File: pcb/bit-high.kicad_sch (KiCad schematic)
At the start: 5 parts, among them Q1 2N7002b, Q2 2N7002b

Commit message: Bit low/high.
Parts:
- renumbered C5 to C19, Q1 to Q707, Q2 to Q708, R1 to R299, R2 to R300
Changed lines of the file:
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@@
     (effects (font (size 1.27 1.27)) (justify left))
   )
-  (symbol (lib_id "power:VCC") (at 184.15 44.45 0) (unit 1)
+  (symbol (lib_id "power:VCC") (at 184.15 44.45 0)
     (in_bom yes) (on_board yes)
-    (property "Reference" "#PWR034" (id 0) (at 184.15 48.26 0)
+    (property "Reference" "#PWR0618" (id 0) (at 184.15 48.26 0)
       (effects (font (size 1.27 1.27)) hide)
     )
@@
     (pin "1")
   )
-  (symbol (lib_id "power:VCC") (at 200.66 40.64 0) (unit 1)
+  (symbol (lib_id "power:VCC") (at 200.66 40.64 0)
     (in_bom yes) (on_board yes)
-    (property "Reference" "#PWR033" (id 0) (at 200.66 44.45 0)
+    (property "Reference" "#PWR0617" (id 0) (at 200.66 44.45 0)
       (effects (font (size 1.27 1.27)) hide)
     )
@@
     (pin "1")
   )
-  (symbol (lib_id "power:VCC") (at 220.98 71.12 0) (unit 1)
+  (symbol (lib_id "power:VCC") (at 220.98 71.12 0)
     (in_bom yes) (on_board yes)
-    (property "Reference" "#PWR036" (id 0) (at 220.98 74.93 0)
+    (property "Reference" "#PWR0620" (id 0) (at 220.98 74.93 0)
       (effects (font (size 1.27 1.27)) hide)
     )
@@
     (pin "1")
   )
-  (symbol (lib_id "power:GND") (at 184.15 52.07 0) (unit 1)
+  (symbol (lib_id "power:GND") (at 184.15 52.07 0)
     (in_bom yes) (on_board yes)
-    (property "Reference" "#PWR035" (id 0) (at 184.15 58.42 0)
+    (property "Reference" "#PWR0619" (id 0) (at 184.15 58.42 0)
       (effects (font (size 1.27 1.27)) hide)
     )
@@
     (pin "1")
   )
-  (symbol (lib_id "power:GND") (at 220.98 109.22 0) (unit 1)
+  (symbol (lib_id "power:GND") (at 220.98 109.22 0)
     (in_bom yes) (on_board yes)
-    (property "Reference" "#PWR037" (id 0) (at 220.98 115.57 0)
+    (property "Reference" "#PWR0621" (id 0) (at 220.98 115.57 0)
       (effects (font (size 1.27 1.27)) hide)
     )
@@
     (pin "1")
   )
-  (symbol (lib_id "Device:R") (at 200.66 44.45 0) (unit 1)
+  (symbol (lib_id "Device:R") (at 200.66 44.45 0)
     (in_bom yes) (on_board yes)
-    (property "Reference" "R1" (id 0) (at 202.438 43.2816 0)
+    (property "Reference" "R299" (id 0) (at 202.438 43.2816 0)
       (effects (font (size 1.27 1.27)) (justify left))
     )
@@
     (pin "2")
   )
-  (symbol (lib_id "Device:R") (at 220.98 74.93 0) (unit 1)
+  (symbol (lib_id "Device:R") (at 220.98 74.93 0)
     (in_bom yes) (on_board yes)
-    (property "Reference" "R2" (id 0) (at 222.758 73.7616 0)
+    (property "Reference" "R300" (id 0) (at 222.758 73.7616 0)
       (effects (font (size 1.27 1.27)) (justify left))
     )
@@
     (pin "2")
   )
-  (symbol (lib_id "Device:C") (at 184.15 48.26 0) (unit 1)
+  (symbol (lib_id "Device:C") (at 184.15 48.26 0)
     (in_bom yes) (on_board yes)
-    (property "Reference" "C5" (id 0) (at 187.071 47.0916 0)
+    (property "Reference" "C19" (id 0) (at 187.071 47.0916 0)
       (effects (font (size 1.27 1.27)) (justify left))
     )
@@
     (pin "2")
   )
-  (symbol (lib_id "Transistor_FET:2N7002") (at 218.44 93.98 0) (unit 1)
+  (symbol (lib_id "Transistor_FET:2N7002") (at 218.44 93.98 0)
     (in_bom yes) (on_board yes)
-    (property "Reference" "Q1" (id 0) (at 223.6724 92.8116 0)
+    (property "Reference" "Q707" (id 0) (at 223.6724 92.8116 0)
       (effects (font (size 1.27 1.27)) (justify left))
     )
@@
     (pin "3")
   )
-  (symbol (lib_id "Transistor_FET:2N7002") (at 218.44 104.14 0) (unit 1)
+  (symbol (lib_id "Transistor_FET:2N7002") (at 218.44 104.14 0)
     (in_bom yes) (on_board yes)
-    (property "Reference" "Q2" (id 0) (at 223.6724 102.9716 0)
+    (property "Reference" "Q708" (id 0) (at 223.6724 102.9716 0)
       (effects (font (size 1.27 1.27)) (justify left))
     )

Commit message: XH/XL.
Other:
- sheet X Register: file xreg.kicad_sch -> xhreg.kicad_sch
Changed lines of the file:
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@@
       (effects (font (size 1.27 1.27)) (justify left bottom))
     )
-    (property "Sheet file" "xreg.kicad_sch" (id 1) (at 110.49 75.4385 0)
+    (property "Sheet file" "xhreg.kicad_sch" (id 1) (at 110.49 75.439 0)
       (effects (font (size 1.27 1.27)) (justify left top))
     )

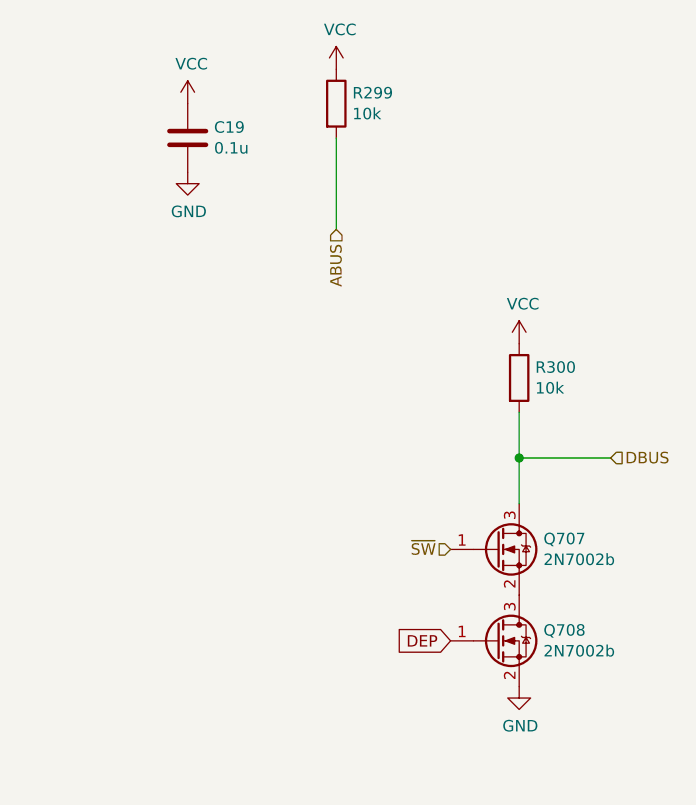
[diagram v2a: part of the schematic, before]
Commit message: Fix UUIDs.
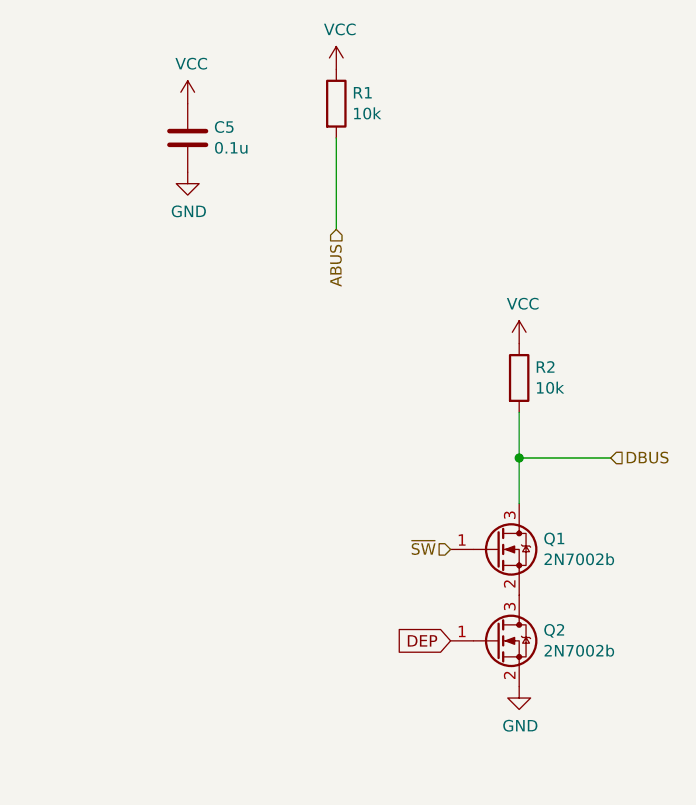
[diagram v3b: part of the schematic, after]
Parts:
- removed C19: 0.1u, Capacitor_SMD:C_0805_2012Metric, symbol Device:C
- removed Q707, Q708: 2N7002b, Package_TO_SOT_SMD:SOT-23, symbol Transistor_FET:2N7002
- removed R299, R300: 10k, Resistor_SMD:R_0805_2012Metric, symbol Device:R
- added C5: 0.1u, Capacitor_SMD:C_0805_2012Metric, symbol Device:C
- added Q1, Q2: 2N7002b, Package_TO_SOT_SMD:SOT-23, symbol Transistor_FET:2N7002
- added R1, R2: 10k, Resistor_SMD:R_0805_2012Metric, symbol Device:R
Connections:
- net ABUS: now also R1.2
- net DBUS: now also Q1.3 (D), R2.2
- net DEP: now also Q2.1 (G)
- net GND: now also C5.2, Q2.2 (S)
- net VCC: now also C5.1, R1.1, R2.1
- net ~SW: now also Q1.1 (G)
- new net: Q1.2 (S), Q2.3 (D)
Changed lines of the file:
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@@
   (symbol (lib_id "power:VCC") (at 184.15 44.45 0)
     (in_bom yes) (on_board yes)
-    (property "Reference" "#PWR0618" (id 0) (at 184.15 48.26 0)
+    (property "Reference" "#PWR020" (id 0) (at 184.15 48.26 0)
       (effects (font (size 1.27 1.27)) hide)
     )
@@
   (symbol (lib_id "power:VCC") (at 200.66 40.64 0)
     (in_bom yes) (on_board yes)
-    (property "Reference" "#PWR0617" (id 0) (at 200.66 44.45 0)
+    (property "Reference" "#PWR019" (id 0) (at 200.66 44.45 0)
       (effects (font (size 1.27 1.27)) hide)
     )
@@
   (symbol (lib_id "power:VCC") (at 220.98 71.12 0)
     (in_bom yes) (on_board yes)
-    (property "Reference" "#PWR0620" (id 0) (at 220.98 74.93 0)
+    (property "Reference" "#PWR022" (id 0) (at 220.98 74.93 0)
       (effects (font (size 1.27 1.27)) hide)
     )
@@
   (symbol (lib_id "power:GND") (at 184.15 52.07 0)
     (in_bom yes) (on_board yes)
-    (property "Reference" "#PWR0619" (id 0) (at 184.15 58.42 0)
+    (property "Reference" "#PWR021" (id 0) (at 184.15 58.42 0)
       (effects (font (size 1.27 1.27)) hide)
     )
@@
   (symbol (lib_id "power:GND") (at 220.98 109.22 0)
     (in_bom yes) (on_board yes)
-    (property "Reference" "#PWR0621" (id 0) (at 220.98 115.57 0)
+    (property "Reference" "#PWR023" (id 0) (at 220.98 115.57 0)
       (effects (font (size 1.27 1.27)) hide)
     )
@@
   (symbol (lib_id "Device:R") (at 200.66 44.45 0)
     (in_bom yes) (on_board yes)
-    (property "Reference" "R299" (id 0) (at 202.438 43.2816 0)
+    (property "Reference" "R1" (id 0) (at 202.438 43.2816 0)
       (effects (font (size 1.27 1.27)) (justify left))
     )
@@
   (symbol (lib_id "Device:R") (at 220.98 74.93 0)
     (in_bom yes) (on_board yes)
-    (property "Reference" "R300" (id 0) (at 222.758 73.7616 0)
+    (property "Reference" "R2" (id 0) (at 222.758 73.7616 0)
       (effects (font (size 1.27 1.27)) (justify left))
     )
@@
   (symbol (lib_id "Device:C") (at 184.15 48.26 0)
     (in_bom yes) (on_board yes)
-    (property "Reference" "C19" (id 0) (at 187.071 47.0916 0)
+    (property "Reference" "C5" (id 0) (at 187.071 47.0916 0)
       (effects (font (size 1.27 1.27)) (justify left))
     )
@@
   (symbol (lib_id "Transistor_FET:2N7002") (at 218.44 93.98 0)
     (in_bom yes) (on_board yes)
-    (property "Reference" "Q707" (id 0) (at 223.6724 92.8116 0)
+    (property "Reference" "Q1" (id 0) (at 223.6724 92.8116 0)
       (effects (font (size 1.27 1.27)) (justify left))
     )
@@
   (symbol (lib_id "Transistor_FET:2N7002") (at 218.44 104.14 0)
     (in_bom yes) (on_board yes)
-    (property "Reference" "Q708" (id 0) (at 223.6724 102.9716 0)
+    (property "Reference" "Q2" (id 0) (at 223.6724 102.9716 0)
       (effects (font (size 1.27 1.27)) (justify left))
     )

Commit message: New reset.
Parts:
- renumbered C5 to C18, Q1 to Q698, Q2 to Q699, R1 to R298, R2 to R299
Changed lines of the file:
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@@
   (symbol (lib_id "power:VCC") (at 184.15 44.45 0)
     (in_bom yes) (on_board yes)
-    (property "Reference" "#PWR020" (id 0) (at 184.15 48.26 0)
+    (property "Reference" "#PWR0596" (id 0) (at 184.15 48.26 0)
       (effects (font (size 1.27 1.27)) hide)
     )
@@
   (symbol (lib_id "power:VCC") (at 200.66 40.64 0)
     (in_bom yes) (on_board yes)
-    (property "Reference" "#PWR019" (id 0) (at 200.66 44.45 0)
+    (property "Reference" "#PWR0595" (id 0) (at 200.66 44.45 0)
       (effects (font (size 1.27 1.27)) hide)
     )
@@
   (symbol (lib_id "power:VCC") (at 220.98 71.12 0)
     (in_bom yes) (on_board yes)
-    (property "Reference" "#PWR022" (id 0) (at 220.98 74.93 0)
+    (property "Reference" "#PWR0598" (id 0) (at 220.98 74.93 0)
       (effects (font (size 1.27 1.27)) hide)
     )
@@
   (symbol (lib_id "power:GND") (at 184.15 52.07 0)
     (in_bom yes) (on_board yes)
-    (property "Reference" "#PWR021" (id 0) (at 184.15 58.42 0)
+    (property "Reference" "#PWR0597" (id 0) (at 184.15 58.42 0)
       (effects (font (size 1.27 1.27)) hide)
     )
@@
   (symbol (lib_id "power:GND") (at 220.98 109.22 0)
     (in_bom yes) (on_board yes)
-    (property "Reference" "#PWR023" (id 0) (at 220.98 115.57 0)
+    (property "Reference" "#PWR0599" (id 0) (at 220.98 115.57 0)
       (effects (font (size 1.27 1.27)) hide)
     )
@@
   (symbol (lib_id "Device:R") (at 200.66 44.45 0)
     (in_bom yes) (on_board yes)
-    (property "Reference" "R1" (id 0) (at 202.438 43.2816 0)
+    (property "Reference" "R298" (id 0) (at 202.438 43.2816 0)
       (effects (font (size 1.27 1.27)) (justify left))
     )
@@
   (symbol (lib_id "Device:R") (at 220.98 74.93 0)
     (in_bom yes) (on_board yes)
-    (property "Reference" "R2" (id 0) (at 222.758 73.7616 0)
+    (property "Reference" "R299" (id 0) (at 222.758 73.7616 0)
       (effects (font (size 1.27 1.27)) (justify left))
     )
@@
   (symbol (lib_id "Device:C") (at 184.15 48.26 0)
     (in_bom yes) (on_board yes)
-    (property "Reference" "C5" (id 0) (at 187.071 47.0916 0)
+    (property "Reference" "C18" (id 0) (at 187.071 47.0916 0)
       (effects (font (size 1.27 1.27)) (justify left))
     )
@@
   (symbol (lib_id "Transistor_FET:2N7002") (at 218.44 93.98 0)
     (in_bom yes) (on_board yes)
-    (property "Reference" "Q1" (id 0) (at 223.6724 92.8116 0)
+    (property "Reference" "Q698" (id 0) (at 223.6724 92.8116 0)
       (effects (font (size 1.27 1.27)) (justify left))
     )
@@
   (symbol (lib_id "Transistor_FET:2N7002") (at 218.44 104.14 0)
     (in_bom yes) (on_board yes)
-    (property "Reference" "Q2" (id 0) (at 223.6724 102.9716 0)
+    (property "Reference" "Q699" (id 0) (at 223.6724 102.9716 0)
       (effects (font (size 1.27 1.27)) (justify left))
     )

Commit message: Some fixes.
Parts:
- renumbered C18 to C22, Q698 to Q695, Q699 to Q696, R298 to R302, R299 to R303
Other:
- sheet S Register ports: added CLR; removed none
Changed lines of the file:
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@@
+    (stroke (width 0) (type solid) (color 0 0 0 0))
+  )
+  (wire (pts (xy 104.14 113.03) (xy 110.49 113.03))
     (stroke (width 0) (type solid) (color 0 0 0 0))
   )
@@
   (symbol (lib_id "power:VCC") (at 184.15 44.45 0)
     (in_bom yes) (on_board yes)
-    (property "Reference" "#PWR0596" (id 0) (at 184.15 48.26 0)
+    (property "Reference" "#PWR0607" (id 0) (at 184.15 48.26 0)
       (effects (font (size 1.27 1.27)) hide)
     )
@@
   (symbol (lib_id "power:VCC") (at 200.66 40.64 0)
     (in_bom yes) (on_board yes)
-    (property "Reference" "#PWR0595" (id 0) (at 200.66 44.45 0)
+    (property "Reference" "#PWR0606" (id 0) (at 200.66 44.45 0)
       (effects (font (size 1.27 1.27)) hide)
     )
@@
   (symbol (lib_id "power:VCC") (at 220.98 71.12 0)
     (in_bom yes) (on_board yes)
-    (property "Reference" "#PWR0598" (id 0) (at 220.98 74.93 0)
+    (property "Reference" "#PWR0609" (id 0) (at 220.98 74.93 0)
       (effects (font (size 1.27 1.27)) hide)
     )
@@
     (pin "1")
   )
+  (symbol (lib_id "power:GND") (at 104.14 113.03 0)
+    (in_bom yes) (on_board yes)
+    (property "Reference" "#PWR0611" (id 0) (at 104.14 119.38 0)
+      (effects (font (size 1.27 1.27)) hide)
+    )
+    (property "Value" "GND" (id 1) (at 104.267 117.4242 0))
+    (property "Footprint" "" (id 2) (at 104.14 113.03 0)
+      (effects (font (size 1.27 1.27)) hide)
+    )
+    (property "Datasheet" "" (id 3) (at 104.14 113.03 0)
+      (effects (font (size 1.27 1.27)) hide)
+    )
+    (pin "1")
+  )
   (symbol (lib_id "power:GND") (at 184.15 52.07 0)
     (in_bom yes) (on_board yes)
-    (property "Reference" "#PWR0597" (id 0) (at 184.15 58.42 0)
+    (property "Reference" "#PWR0608" (id 0) (at 184.15 58.42 0)
       (effects (font (size 1.27 1.27)) hide)
     )
@@
   (symbol (lib_id "power:GND") (at 220.98 109.22 0)
     (in_bom yes) (on_board yes)
-    (property "Reference" "#PWR0599" (id 0) (at 220.98 115.57 0)
+    (property "Reference" "#PWR0610" (id 0) (at 220.98 115.57 0)
       (effects (font (size 1.27 1.27)) hide)
     )
@@
   (symbol (lib_id "Device:R") (at 200.66 44.45 0)
     (in_bom yes) (on_board yes)
-    (property "Reference" "R298" (id 0) (at 202.438 43.2816 0)
+    (property "Reference" "R302" (id 0) (at 202.438 43.2816 0)
       (effects (font (size 1.27 1.27)) (justify left))
     )
@@
   (symbol (lib_id "Device:R") (at 220.98 74.93 0)
     (in_bom yes) (on_board yes)
-    (property "Reference" "R299" (id 0) (at 222.758 73.7616 0)
+    (property "Reference" "R303" (id 0) (at 222.758 73.7616 0)
       (effects (font (size 1.27 1.27)) (justify left))
     )
@@
   (symbol (lib_id "Device:C") (at 184.15 48.26 0)
     (in_bom yes) (on_board yes)
-    (property "Reference" "C18" (id 0) (at 187.071 47.0916 0)
+    (property "Reference" "C22" (id 0) (at 187.071 47.0916 0)
       (effects (font (size 1.27 1.27)) (justify left))
     )
@@
   (symbol (lib_id "Transistor_FET:2N7002") (at 218.44 93.98 0)
     (in_bom yes) (on_board yes)
-    (property "Reference" "Q698" (id 0) (at 223.6724 92.8116 0)
+    (property "Reference" "Q695" (id 0) (at 223.6724 92.8116 0)
       (effects (font (size 1.27 1.27)) (justify left))
     )
@@
   (symbol (lib_id "Transistor_FET:2N7002") (at 218.44 104.14 0)
     (in_bom yes) (on_board yes)
-    (property "Reference" "Q699" (id 0) (at 223.6724 102.9716 0)
+    (property "Reference" "Q696" (id 0) (at 223.6724 102.9716 0)
       (effects (font (size 1.27 1.27)) (justify left))
     )
@@
       (effects (font (size 1.27 1.27)) (justify left))
     )
+    (pin "CLR" input (at 110.49 113.03 180)
+      (effects (font (size 1.27 1.27)) (justify left))
+    )

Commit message: Faster.
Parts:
- renumbered C22 to C21, Q695 to Q693, Q696 to Q694, R302 to R300, R303 to R301
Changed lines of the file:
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@@
   (symbol (lib_id "power:VCC") (at 184.15 44.45 0)
     (in_bom yes) (on_board yes)
-    (property "Reference" "#PWR0607" (id 0) (at 184.15 48.26 0)
+    (property "Reference" "#PWR0604" (id 0) (at 184.15 48.26 0)
       (effects (font (size 1.27 1.27)) hide)
     )
@@
   (symbol (lib_id "power:VCC") (at 200.66 40.64 0)
     (in_bom yes) (on_board yes)
-    (property "Reference" "#PWR0606" (id 0) (at 200.66 44.45 0)
+    (property "Reference" "#PWR0603" (id 0) (at 200.66 44.45 0)
       (effects (font (size 1.27 1.27)) hide)
     )
@@
   (symbol (lib_id "power:VCC") (at 220.98 71.12 0)
     (in_bom yes) (on_board yes)
-    (property "Reference" "#PWR0609" (id 0) (at 220.98 74.93 0)
+    (property "Reference" "#PWR0606" (id 0) (at 220.98 74.93 0)
       (effects (font (size 1.27 1.27)) hide)
     )
@@
   (symbol (lib_id "power:GND") (at 104.14 113.03 0)
     (in_bom yes) (on_board yes)
-    (property "Reference" "#PWR0611" (id 0) (at 104.14 119.38 0)
+    (property "Reference" "#PWR0608" (id 0) (at 104.14 119.38 0)
       (effects (font (size 1.27 1.27)) hide)
     )
@@
   (symbol (lib_id "power:GND") (at 184.15 52.07 0)
     (in_bom yes) (on_board yes)
-    (property "Reference" "#PWR0608" (id 0) (at 184.15 58.42 0)
+    (property "Reference" "#PWR0605" (id 0) (at 184.15 58.42 0)
       (effects (font (size 1.27 1.27)) hide)
     )
@@
   (symbol (lib_id "power:GND") (at 220.98 109.22 0)
     (in_bom yes) (on_board yes)
-    (property "Reference" "#PWR0610" (id 0) (at 220.98 115.57 0)
+    (property "Reference" "#PWR0607" (id 0) (at 220.98 115.57 0)
       (effects (font (size 1.27 1.27)) hide)
     )
@@
   (symbol (lib_id "Device:R") (at 200.66 44.45 0)
     (in_bom yes) (on_board yes)
-    (property "Reference" "R302" (id 0) (at 202.438 43.2816 0)
+    (property "Reference" "R300" (id 0) (at 202.438 43.2816 0)
       (effects (font (size 1.27 1.27)) (justify left))
     )
@@
   (symbol (lib_id "Device:R") (at 220.98 74.93 0)
     (in_bom yes) (on_board yes)
-    (property "Reference" "R303" (id 0) (at 222.758 73.7616 0)
+    (property "Reference" "R301" (id 0) (at 222.758 73.7616 0)
       (effects (font (size 1.27 1.27)) (justify left))
     )
@@
   (symbol (lib_id "Device:C") (at 184.15 48.26 0)
     (in_bom yes) (on_board yes)
-    (property "Reference" "C22" (id 0) (at 187.071 47.0916 0)
+    (property "Reference" "C21" (id 0) (at 187.071 47.0916 0)
       (effects (font (size 1.27 1.27)) (justify left))
     )
@@
   (symbol (lib_id "Transistor_FET:2N7002") (at 218.44 93.98 0)
     (in_bom yes) (on_board yes)
-    (property "Reference" "Q695" (id 0) (at 223.6724 92.8116 0)
+    (property "Reference" "Q693" (id 0) (at 223.6724 92.8116 0)
       (effects (font (size 1.27 1.27)) (justify left))
     )
@@
   (symbol (lib_id "Transistor_FET:2N7002") (at 218.44 104.14 0)
     (in_bom yes) (on_board yes)
-    (property "Reference" "Q696" (id 0) (at 223.6724 102.9716 0)
+    (property "Reference" "Q694" (id 0) (at 223.6724 102.9716 0)
       (effects (font (size 1.27 1.27)) (justify left))
     )

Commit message: Updates
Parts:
- Q693, Q694: value 2N7002b -> 2N7002K; LCSC C8545 -> C181083
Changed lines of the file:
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@@
       (effects (font (size 1.27 1.27)) (justify left))
     )
-    (property "Value" "2N7002b" (id 1) (at 223.672 95.123 0)
+    (property "Value" "2N7002K" (id 1) (at 223.672 95.123 0)
       (effects (font (size 1.27 1.27)) (justify left))
     )
@@
       (effects (font (size 1.27 1.27) italic) (justify left) hide)
     )
-    (property "Datasheet" "https://www.fairchildsemi.com/datasheets/2N/2N7002.pdf" (id 3) (at 218.44 93.98 0)
+    (property "Datasheet" "https://datasheet.lcsc.com/szlcsc/Guangdong-Hottech-2N7002K_C181083.pdf" (id 3) (at 218.44 93.98 0)
       (effects (font (size 1.27 1.27)) (justify left) hide)
     )
-    (property "LCSC" "C8545" (id 4) (at 218.44 93.98 0)
+    (property "LCSC" "C181083" (id 4) (at 218.44 93.98 0)
       (effects (font (size 1.27 1.27)) hide)
     )
@@
       (effects (font (size 1.27 1.27)) (justify left))
     )
-    (property "Value" "2N7002b" (id 1) (at 223.672 105.283 0)
+    (property "Value" "2N7002K" (id 1) (at 223.672 105.283 0)
       (effects (font (size 1.27 1.27)) (justify left))
     )
@@
       (effects (font (size 1.27 1.27) italic) (justify left) hide)
     )
-    (property "Datasheet" "https://www.fairchildsemi.com/datasheets/2N/2N7002.pdf" (id 3) (at 218.44 104.14 0)
+    (property "Datasheet" "https://datasheet.lcsc.com/szlcsc/Guangdong-Hottech-2N7002K_C181083.pdf" (id 3) (at 218.44 104.14 0)
       (effects (font (size 1.27 1.27)) (justify left) hide)
     )
-    (property "LCSC" "C8545" (id 4) (at 218.44 104.14 0)
+    (property "LCSC" "C181083" (id 4) (at 218.44 104.14 0)
       (effects (font (size 1.27 1.27)) hide)
     )
